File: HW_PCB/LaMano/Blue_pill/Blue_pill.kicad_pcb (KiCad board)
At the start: 2 copper layers, 38.6 x 55.1 mm, 28 parts, among them J1 V_Battery, J2 STLINK, J5 MPU6050, J6 NRF24, SW1 SW_DPST_x2, SW2 SW_DPST_x2, U1 STM32F103C8Tx, U2 AMS1117-3.3, X1 Crystal

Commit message: Modified Placa Mano
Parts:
- J5: footprint Connector_PinHeader_1.00mm:PinHeader_1x08_P1.00mm_Vertical -> Connector_PinSocket_2.54mm:PinSocket_1x08_P2.54mm_Vertical
- moved SW1 15.8 mm to (68.6, 81.1), turned to 180 degrees
- moved D1 13.5 mm to (43.7, 73.0), turned to 0 degrees
- moved J5 11.7 mm to (38.0, 50.8)
- moved D2 10.8 mm to (43.8, 75.8), turned to 0 degrees
- moved R3 10.5 mm to (47.9, 73.0), turned to 180 degrees
- moved C7 9.96 mm to (55.7, 48.5), turned to 0 degrees
- moved D3 9.16 mm to (43.8, 78.3), turned to 0 degrees
- moved J1 8.14 mm to (52.0, 44.6)
- moved R5 6.78 mm to (47.9, 75.8), turned to 180 degrees
- moved R4 5.22 mm to (63.8, 75.8), turned to -90 degrees
- moved R6 4.10 mm to (47.8, 78.3), turned to 180 degrees
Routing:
- net GND: track 99.5 -> 68.1 mm
- net IRQ: track 0.00 -> 10.2 mm
- net RED: track 21.5 -> 11.7 mm
- net VCC: track 108.9 -> 100.4 mm
- net YELLOW: track 21.4 -> 16.2 mm
- net SWCLK: track 10.4 -> 13.5 mm
- net GREEN: track 20.6 -> 17.8 mm
- net VIN: track 8.51 -> 10.9 mm
- net NRST: track 24.5 -> 23.3 mm
- net unconnected-(U1-PA15-Pad38): track 1.00 -> 0.00 mm
- removed copper zone on F.Cu, net GND

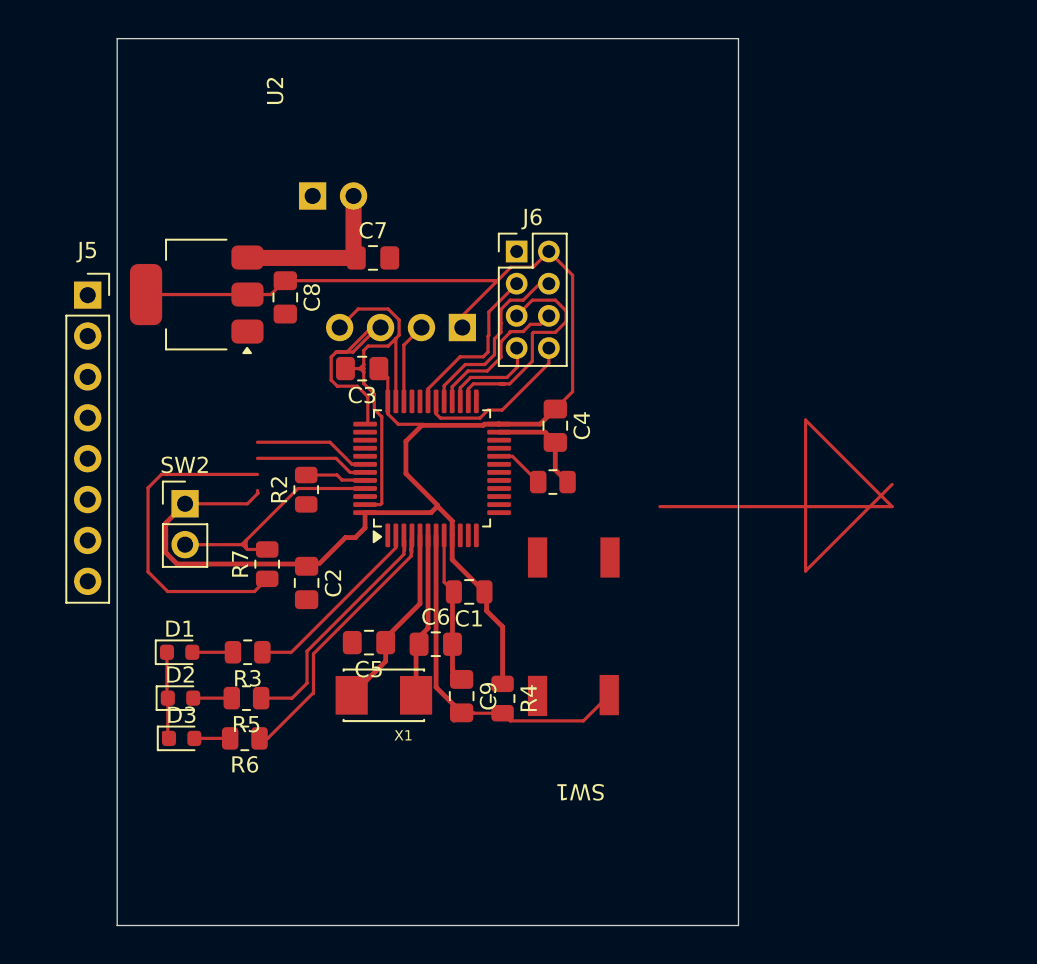
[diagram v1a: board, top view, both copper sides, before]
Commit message: Pending to add MPU6050 Footprint
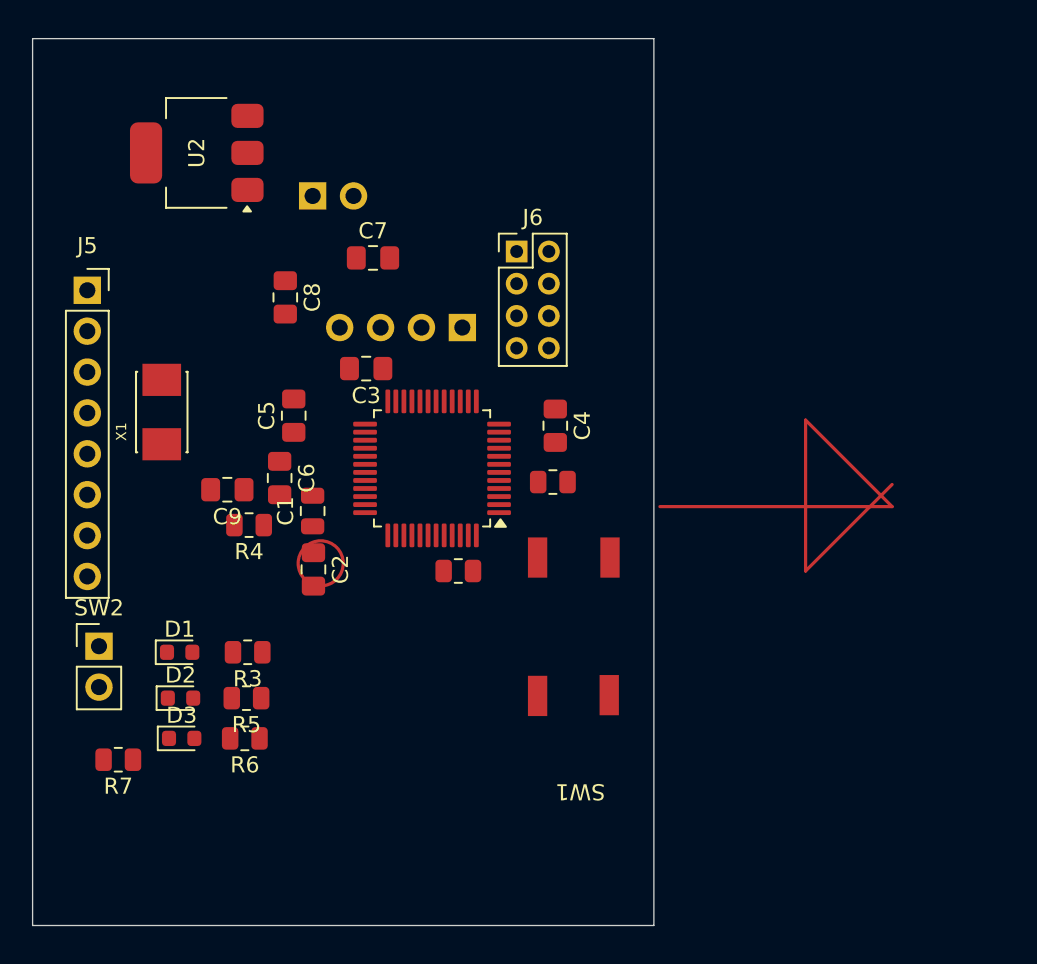
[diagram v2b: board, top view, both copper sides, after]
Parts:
- moved X1 22.4 mm to (42.6, 58.0), turned to 90 degrees
- moved C9 19.4 mm to (46.7, 62.9), turned to 180 degrees
- moved R4 19.1 mm to (48.0, 65.1), turned to 180 degrees
- moved R7 15.3 mm to (39.9, 79.7), turned to 180 degrees
- moved C5 14.9 mm to (50.8, 58.3), turned to 90 degrees
- moved C6 14.2 mm to (49.9, 62.1), turned to -90 degrees
- moved C1 10.9 mm to (52.0, 64.2), turned to 90 degrees
- moved R2 10.7 mm to (61.0, 67.9), turned to 180 degrees
- moved SW2 10.3 mm to (38.7, 72.6)
- moved U2 8.80 mm to (44.8, 42.0)
- moved C2 0.95 mm to (52.0, 67.8)
- moved J5 0.30 mm to (38.0, 50.5)
- moved C3 0.25 mm to (55.3, 55.4)
- turned U1 to 180 degrees
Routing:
- net VCC: track 100.4 -> 0.00 mm
- net GND: track 68.1 -> 0.00 mm
- net NRST: track 23.3 -> 0.00 mm
- net GREEN: track 17.8 -> 0.00 mm
- net YELLOW: track 16.2 -> 0.00 mm
- net SW_LUZ: track 14.8 -> 0.00 mm
- net SCK: track 14.5 -> 0.00 mm
- net SWCLK: track 13.5 -> 0.00 mm
- net RED: track 11.7 -> 0.00 mm
- net OSC_IN: track 11.7 -> 0.00 mm
- net CSN: track 11.6 -> 0.00 mm
- net VIN: track 10.9 -> 0.00 mm
- net CE: track 10.8 -> 0.00 mm
- net OSC_OUT: track 10.5 -> 0.00 mm
- net IRQ: track 10.2 -> 0.00 mm
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
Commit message: Updated Kicad
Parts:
- moved U2 35.9 mm to (57.6, 75.5), turned to 90 degrees
- moved J1 35.5 mm to (72.2, 73.8), turned to 180 degrees
- moved SW1 31.6 mm to (37.4, 75.9), turned to 90 degrees
- moved C7 31.2 mm to (63.6, 78.7)
- moved C8 30.8 mm to (54.0, 81.5), turned to 180 degrees
- moved R7 30.3 mm to (56.3, 54.2), turned to -90 degrees
- moved D3 30.2 mm to (41.7, 48.2), turned to -90 degrees
- moved SW2 28.6 mm to (53.5, 48.2), turned to 90 degrees
- moved D2 27.7 mm to (44.2, 48.1), turned to -90 degrees
- moved R6 26.8 mm to (41.7, 52.2), turned to 90 degrees
- moved D1 25.2 mm to (47.0, 48.0), turned to -90 degrees
- moved R5 23.9 mm to (44.2, 52.2), turned to 90 degrees
- moved R3 20.8 mm to (47.0, 52.2), turned to 90 degrees
- moved C2 18.1 mm to (63.8, 81.6), turned to 0 degrees
- moved R2 14.1 mm to (58.4, 54.1), turned to -90 degrees
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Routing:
- net VCC: track 0.00 -> 29.1 mm
- net GREEN: track 0.00 -> 17.2 mm
- net IRQ: track 0.00 -> 15.8 mm
- net YELLOW: track 0.00 -> 15.3 mm
- net VIN: track 0.00 -> 13.3 mm
- net OSC_IN: track 0.00 -> 12.9 mm
- net SCK: track 0.00 -> 11.7 mm
- net SW_LUZ: track 0.00 -> 11.6 mm
- net RED: track 0.00 -> 11.1 mm
- net OSC_OUT: track 0.00 -> 10.5 mm
- net SWDIO: track 0.00 -> 10.1 mm
- net CSN: track 0.00 -> 9.06 mm
- net MOSI: track 0.00 -> 8.82 mm
- net MISO: track 0.00 -> 7.44 mm
- net SWCLK: track 0.00 -> 7.00 mm
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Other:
- board size 38.6 x 55.1 mm -> 38.6 x 42.8 mm

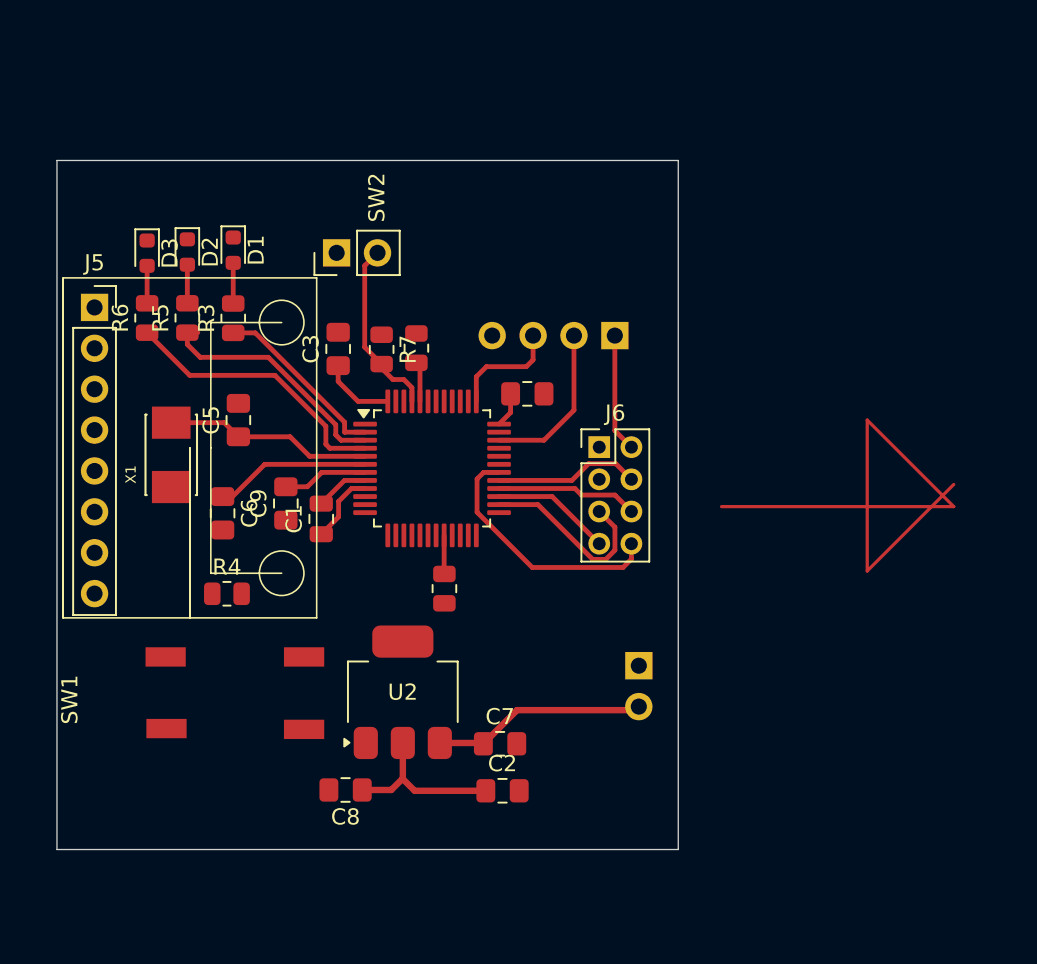
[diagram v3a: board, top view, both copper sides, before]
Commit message: Pending to route voltage tracks
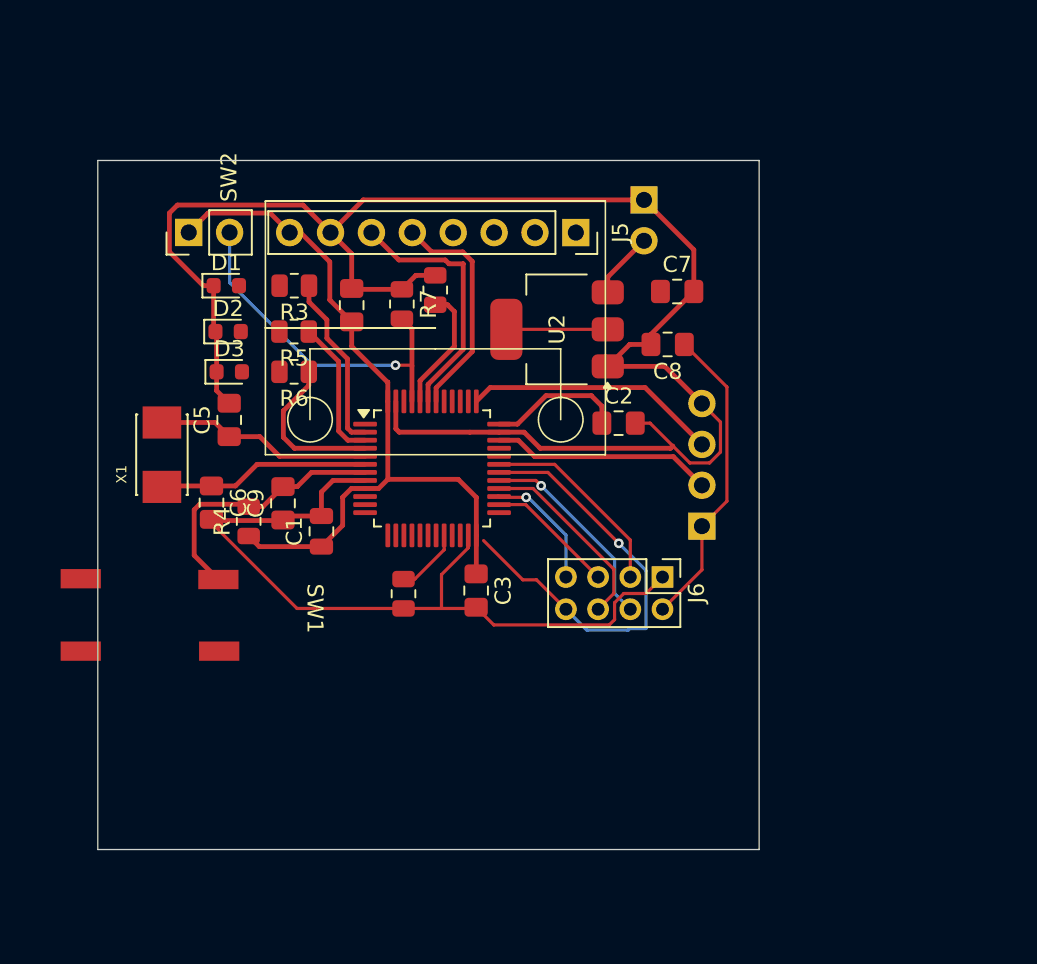
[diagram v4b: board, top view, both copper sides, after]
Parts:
- moved C8 34.2 mm to (74.0, 53.9)
- moved J5 30.3 mm to (68.3, 46.9), turned to -90 degrees
- moved C7 30.2 mm to (74.6, 50.6)
- moved J1 28.9 mm to (72.6, 44.9)
- moved U2 24.5 mm to (67.2, 52.9), turned to 180 degrees
- moved C2 24.0 mm to (71.0, 58.7)
- moved C3 17.3 mm to (62.1, 69.1), turned to -90 degrees
- moved SW1 15.3 mm to (51.6, 70.3), turned to -90 degrees
- moved J2 13.0 mm to (76.2, 65.1), turned to 0 degrees
- moved C4 12.2 mm to (54.4, 51.4), turned to 90 degrees
- moved R6 9.72 mm to (50.8, 55.5), turned to 180 degrees
- moved SW2 9.28 mm to (44.3, 46.9)
- moved J6 8.98 mm to (73.7, 68.3), turned to -90 degrees
- moved D3 8.97 mm to (46.8, 55.5), turned to 0 degrees
- moved R5 6.68 mm to (50.8, 53.0), turned to 180 degrees
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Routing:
- net GND: track 3.32 -> 155.0 mm
- net VCC: track 29.1 -> 81.9 mm
- net SCL: track 0.00 -> 16.0 mm
- net SDA: track 0.00 -> 14.1 mm
- net CE: track 0.00 -> 12.4 mm
- net IRQ: track 15.8 -> 27.7 mm, vias 0 -> 1
- net NRST: track 5.29 -> 16.7 mm
- net SW_LUZ: track 11.6 -> 22.0 mm, vias 0 -> 1
- net VIN: track 13.3 -> 4.13 mm
- net SWCLK: track 7.00 -> 15.8 mm
- net GREEN: track 17.2 -> 10.1 mm
- net YELLOW: track 15.3 -> 8.83 mm
- net Net-(U1-BOOT0): track 2.49 -> 7.83 mm
- net SWDIO: track 10.1 -> 13.8 mm
- net CSN: track 9.06 -> 12.7 mm, vias 0 -> 1
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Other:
- board size 38.6 x 42.8 mm -> 41.1 x 42.8 mm

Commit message: Small Joshua Changes
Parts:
- moved SW1 5.26 mm to (56.9, 70.3)
- moved C8 1.07 mm to (74.6, 53.0), turned to 0 degrees
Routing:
- net VCC: track 81.9 -> 108.8 mm, vias 0 -> 3
- net IRQ: track 27.7 -> 15.1 mm
- net GND: track 155.0 -> 167.3 mm, vias 0 -> 1
- net SWDIO: track 13.8 -> 24.2 mm
- net NRST: track 16.7 -> 25.2 mm, vias 0 -> 2
- net SW_LUZ: track 22.0 -> 19.4 mm
- net Net-(D1-A): track 0.00 -> 2.52 mm
- net Net-(D2-A): track 0.00 -> 2.40 mm
- net Net-(D3-A): track 0.00 -> 2.33 mm
- net VIN: track 4.13 -> 6.27 mm
- net Net-(U1-BOOT0): track 7.83 -> 6.40 mm
- net SDA: track 14.1 -> 12.8 mm
- net SCL: track 16.0 -> 14.8 mm
- net SWCLK: track 15.8 -> 15.9 mm, vias 0 -> 1

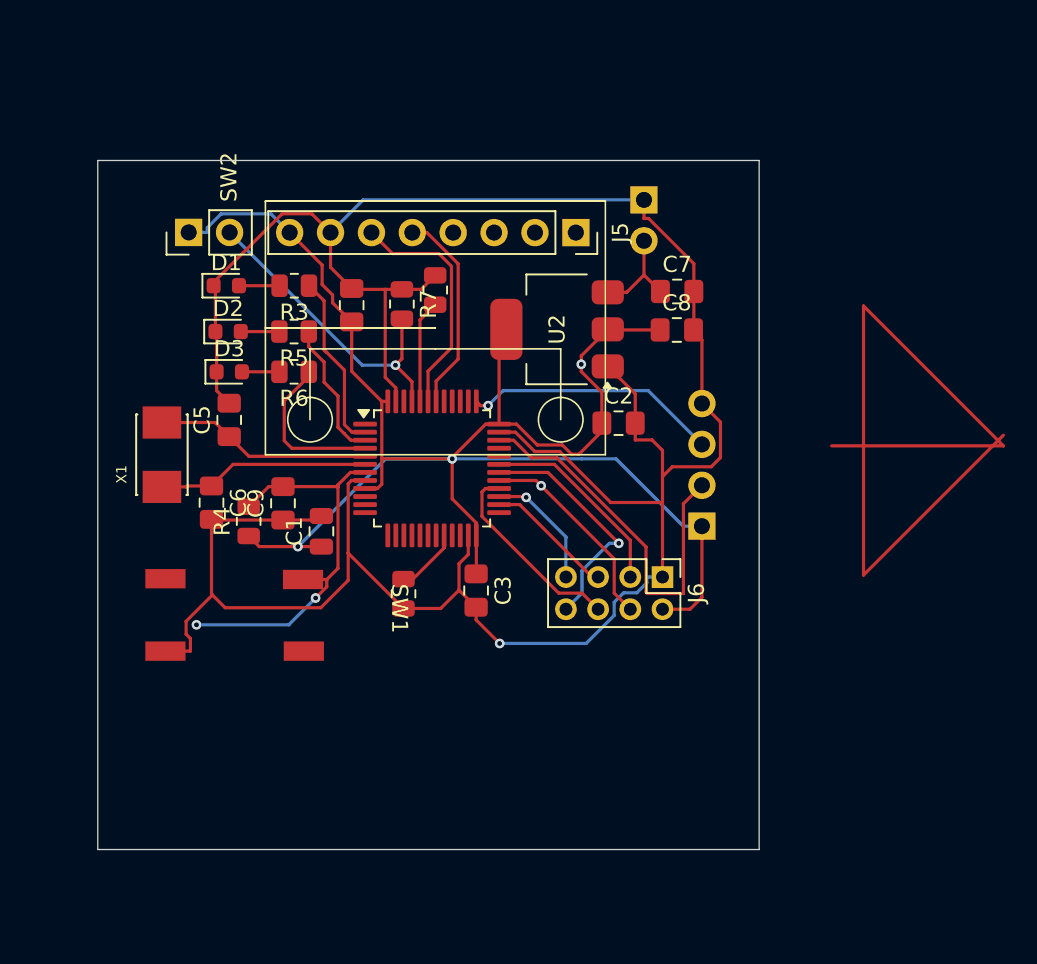
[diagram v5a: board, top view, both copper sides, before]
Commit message: Pending to route voltages, expected to do one side
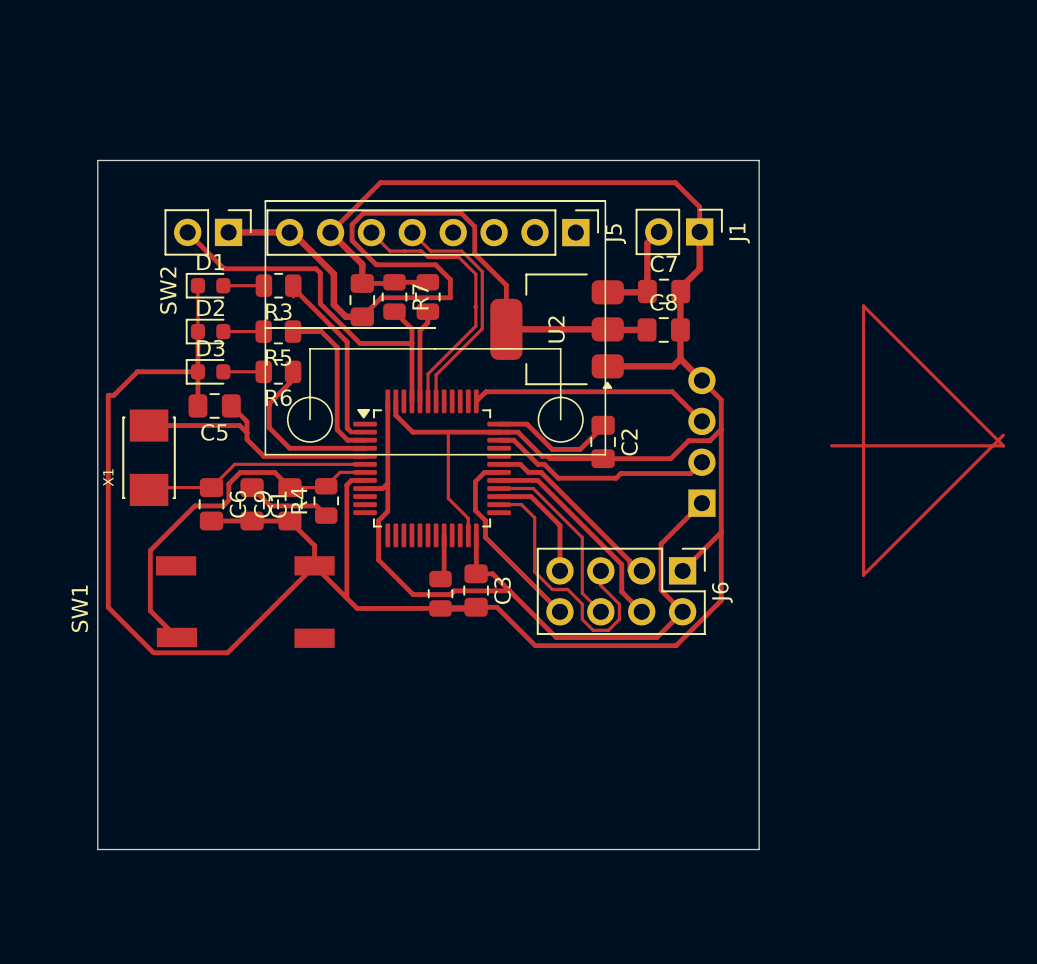
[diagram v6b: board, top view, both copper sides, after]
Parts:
- C1: footprint Capacitor_SMD:C_0805_2012Metric -> Capacitor_SMD:C_0805_2012Metric_Pad1.18x1.45mm_HandSolder
- J1: moved to F.Cu
- J5: footprint Connector_PinSocket_2.54mm:PinSocket_1x08_P2.54mm_Vertical -> Connector_PinHeader_2.54mm:PinHeader_1x08_P2.54mm_Vertical
- J6: footprint Connector_PinHeader_2.00mm:PinHeader_2x04_P2.00mm_Vertical -> Connector_PinHeader_2.54mm:PinHeader_2x04_P2.54mm_Vertical
- moved SW1 18.8 mm to (38.0, 70.3), turned to 90 degrees
- moved R4 4.98 mm to (52.8, 63.6)
- moved C1 4.62 mm to (48.2, 63.8), turned to -90 degrees
- moved J1 3.99 mm to (76.0, 46.9), turned to -90 degrees
- moved SW2 2.48 mm to (46.8, 46.9), turned to -90 degrees
- moved R1 2.30 mm to (59.9, 69.3)
- moved C2 1.51 mm to (70.0, 59.9), turned to -90 degrees
- moved J2 1.43 mm to (76.2, 63.7)
- moved J6 1.31 mm to (75.0, 67.9)
- moved C5 1.26 mm to (45.9, 57.7), turned to 180 degrees
- moved D3 1.16 mm to (45.6, 55.5)
- moved D2 1.09 mm to (45.6, 53.0)
- moved D1 0.98 mm to (45.6, 50.2)
- moved R3 0.98 mm to (49.9, 50.2)
- moved R5 0.98 mm to (49.8, 53.0)
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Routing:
- net GND: track 167.3 -> 185.2 mm, vias 1 -> 0
- net SWDIO: track 24.2 -> 14.0 mm
- net SCK: track 8.02 -> 17.0 mm
- net SW_LUZ: track 19.4 -> 23.9 mm, vias 1 -> 0
- net OSC_IN: track 13.5 -> 16.5 mm
- net NRST: track 25.2 -> 22.8 mm, vias 2 -> 0
- net IRQ: track 15.1 -> 12.7 mm, vias 1 -> 0
- net VCC: track 108.8 -> 111.0 mm, vias 3 -> 0
- net SCL: track 14.8 -> 16.7 mm
- net SDA: track 12.8 -> 14.6 mm
- net YELLOW: track 8.72 -> 10.3 mm
- net Net-(U1-PB2): track 4.10 -> 2.81 mm
- net OSC_OUT: track 13.2 -> 14.3 mm
- net RED: track 11.3 -> 12.1 mm
- net SWCLK: track 15.9 -> 15.0 mm, vias 1 -> 0
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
